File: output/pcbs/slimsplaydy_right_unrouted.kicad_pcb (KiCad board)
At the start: 2 copper layers, 117.1 x 87.4 mm, 24 parts

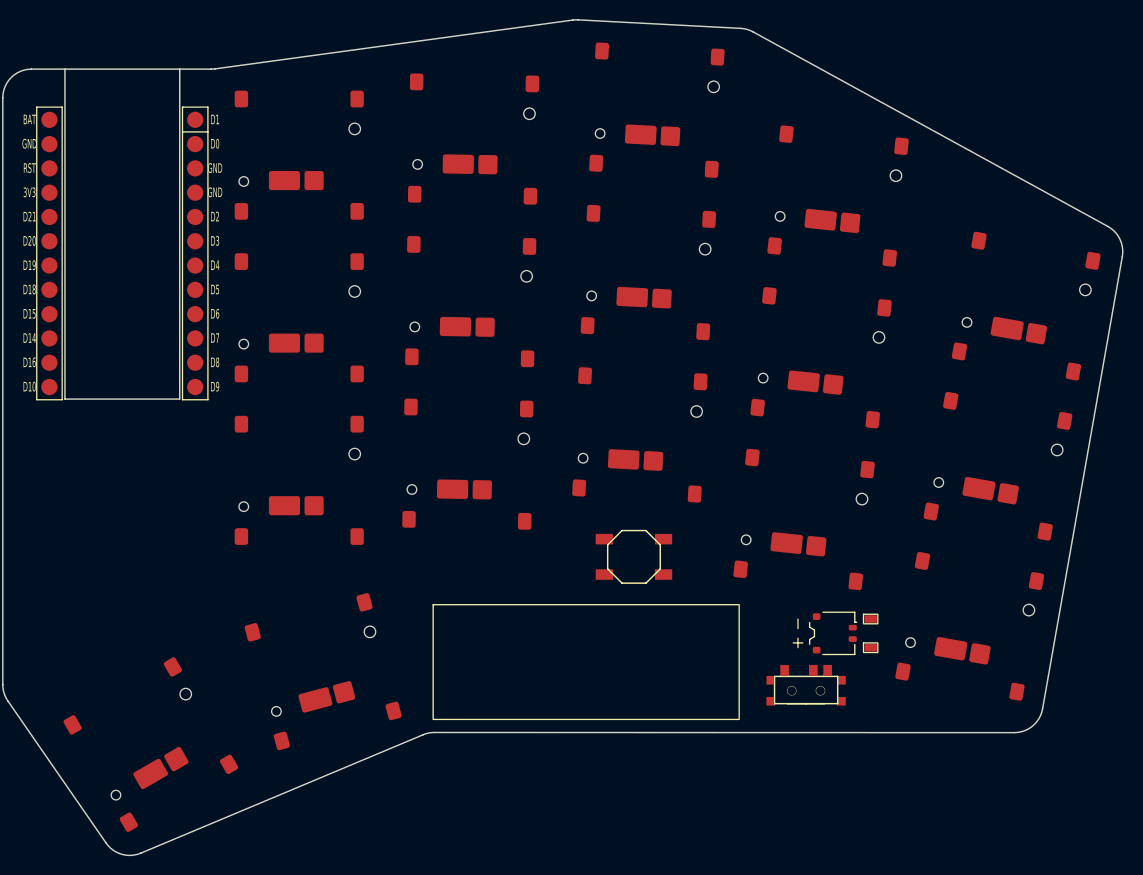
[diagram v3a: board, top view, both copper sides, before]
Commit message: Change weird 5/28 roundrect ratios to 1/8
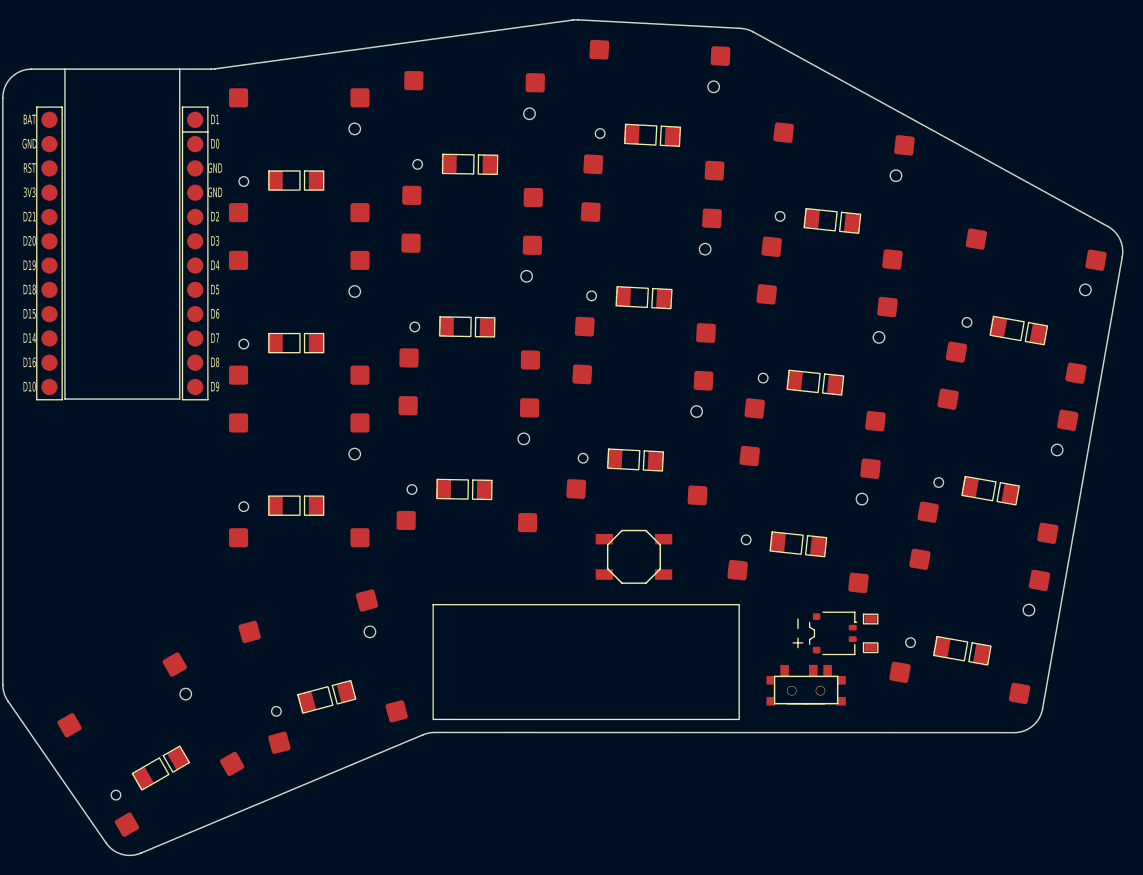
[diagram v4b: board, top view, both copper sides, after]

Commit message: Add logic to only place vias once when board is reversible; fix mispellings of reversible.
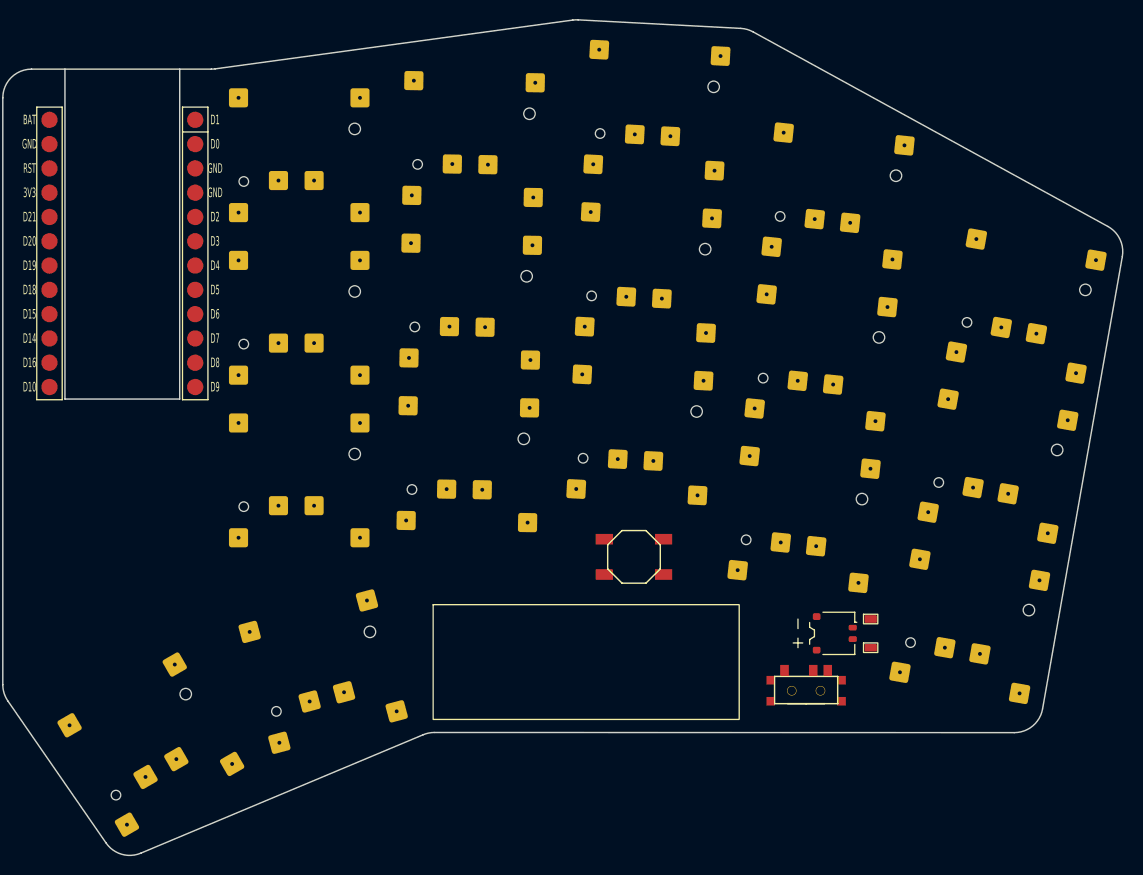
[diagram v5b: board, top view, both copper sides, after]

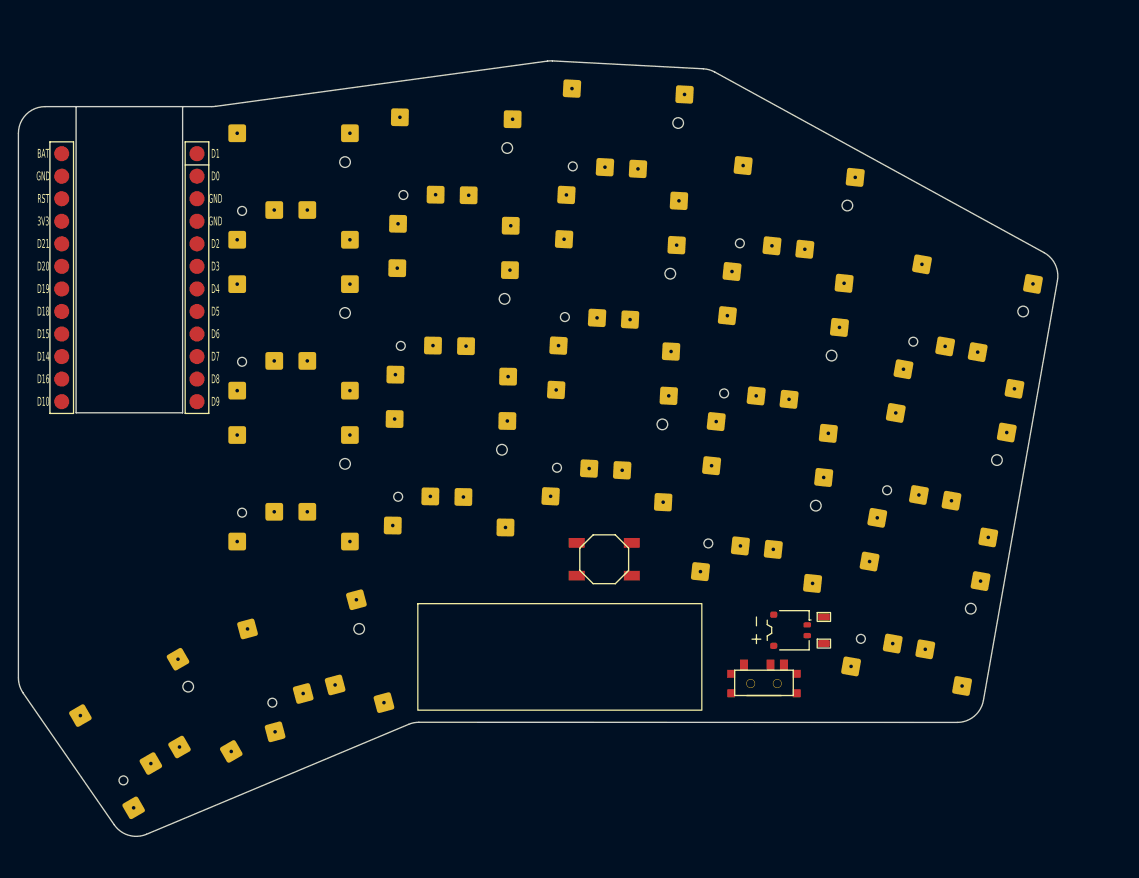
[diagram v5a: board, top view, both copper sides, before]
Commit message: Reposition battery/connector, work on mounting holes.
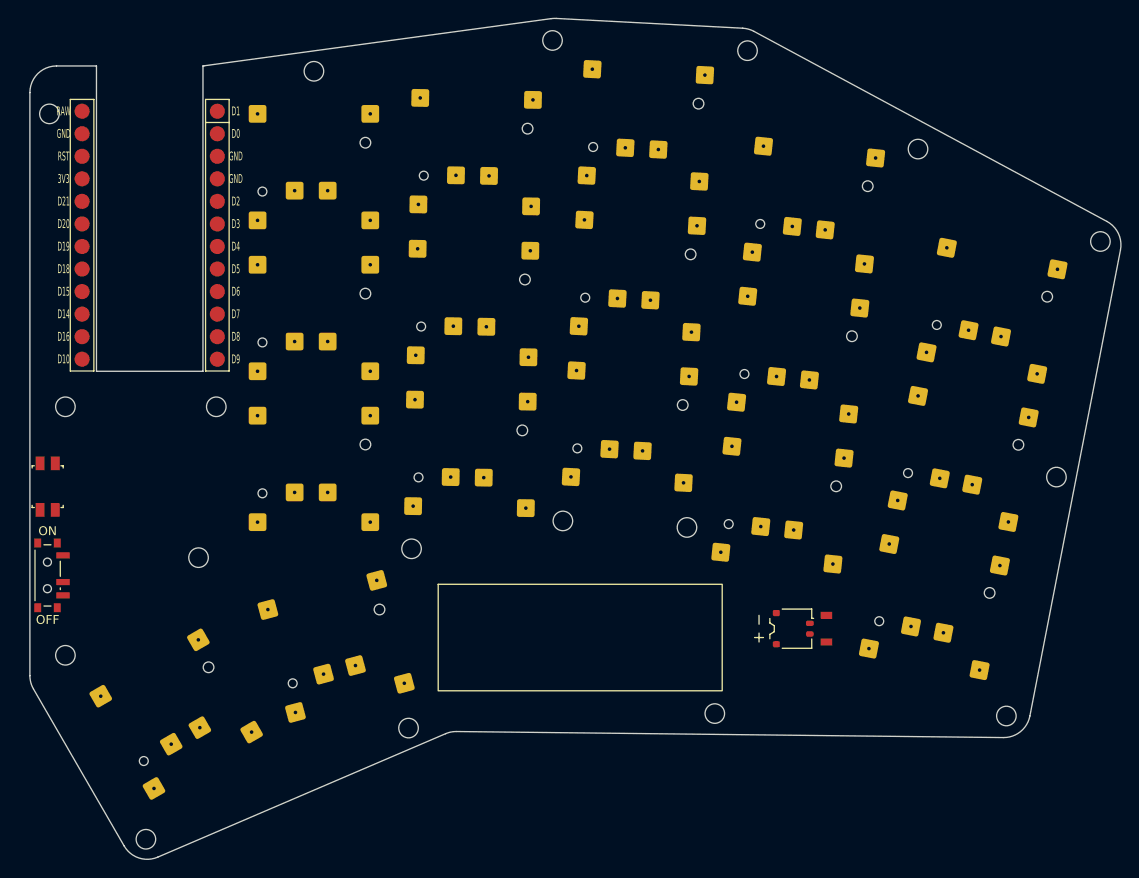
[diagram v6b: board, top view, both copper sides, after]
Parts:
- removed B1: , E73:SW_TACT_ALPS_SKQGABE010
- removed T1: , E73:SPDT_C128955
- removed XX2: , Pad_Single
- removed XX3: , Battery_301230
- added MH1: , ceoloide:mounting_hole_npth, F.Cu at (261.0, 81.4)
- added MH10: , ceoloide:mounting_hole_npth, F.Cu at (289.1, 132.1)
- added MH11: , ceoloide:mounting_hole_npth, F.Cu at (303.0, 132.8)
- added MH12: , ceoloide:mounting_hole_npth, F.Cu at (306.2, 153.8)
- added MH13: , ceoloide:mounting_hole_npth, F.Cu at (339.0, 154.1)
- added MH14: , ceoloide:mounting_hole_npth, F.Cu at (344.7, 127.1)
- added MH15: , ceoloide:mounting_hole_npth, F.Cu at (349.6, 100.6)
- added MH16: , ceoloide:mounting_hole_npth, F.Cu at (329.1, 90.2)
- added MH17: , ceoloide:mounting_hole_npth, F.Cu at (309.9, 79.1)
- added MH18: , ceoloide:mounting_hole_npth, F.Cu at (287.9, 78.0)
- added MH2: , ceoloide:mounting_hole_npth, F.Cu at (231.2, 86.2)
- added MH3: , ceoloide:mounting_hole_npth, F.Cu at (250.0, 119.2)
- added MH4: , ceoloide:mounting_hole_npth, F.Cu at (233.0, 119.2)
- added MH5: , ceoloide:mounting_hole_npth, F.Cu at (248.0, 136.2)
- added MH6: , ceoloide:mounting_hole_npth, F.Cu at (233.0, 147.2)
- added MH7: , ceoloide:mounting_hole_npth, F.Cu at (242.1, 168.0)
- added MH8: , ceoloide:mounting_hole_npth, F.Cu at (271.7, 155.4)
- added MH9: , ceoloide:mounting_hole_npth, F.Cu at (272.0, 135.2)
- added PAD1: , SMDPad, F.Cu at (318.8, 142.7)
- added PAD2: , SMDPad, F.Cu at (318.8, 145.7)
- added PWR1: , ceoloide:power_switch_smd_side, F.Cu at (231.0, 138.2)
- added RST1: , ceoloide:reset_switch_smd_side, F.Cu at (231.0, 128.2)
- XX1: footprint Pad_Single -> Battery_301230
- moved XX1 27.6 mm to (291.0, 145.2)
- moved MCU1 5.30 mm to (242.5, 98.6)
- moved S3 3.21 mm to (337.4, 108.4), turned to -11 degrees
- moved S6 3.17 mm to (317.3, 96.5)
- moved S15 3.17 mm to (261.0, 92.2)
- moved S4 3.17 mm to (313.8, 130.3)
- moved S13 3.17 mm to (261.0, 126.2)
- moved S14 3.17 mm to (261.0, 109.2)
- moved S16 3.17 mm to (263.5, 146.2)
- moved S5 3.17 mm to (315.6, 113.4)
- moved S7 3.17 mm to (296.6, 121.5)
- moved S9 3.17 mm to (298.4, 87.5)
- moved S8 3.17 mm to (297.5, 104.5)
- moved S17 3.17 mm to (245.5, 153.9)
- moved S12 3.17 mm to (279.2, 90.5)
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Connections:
- MCU1 pad 24: BAT -> RAW
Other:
- board size 117.1 x 87.4 mm -> 122.9 x 94.7 mm

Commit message: Finish up mounting, add case outlines, export step.
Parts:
- moved S12 178.9 mm to (170.2, -51.3)
- moved MH7 178.9 mm to (133.0, 26.2)
- moved S17 178.9 mm to (136.4, 12.1)
- moved MH15 178.9 mm to (240.6, -41.2)
- moved MH12 178.9 mm to (197.1, 12.0)
- moved MH14 178.9 mm to (235.6, -14.6)
- moved MH18 178.9 mm to (178.8, -63.8)
- moved S1 178.9 mm to (221.9, 0.00)
- moved S10 178.9 mm to (169.6, -17.3)
- moved S2 178.9 mm to (225.1, -16.7)
- moved S3 178.9 mm to (228.3, -33.4)
- moved S9 178.9 mm to (189.3, -54.3)
- moved CONN1 178.9 mm to (205.9, 2.43)
- moved MCU1 178.9 mm to (133.4, -43.2)
- moved MH1 178.9 mm to (151.9, -60.4)
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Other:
- net class Default removed

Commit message: Fix bug in PG1316S footprint causing vias in pads to not route correctly.
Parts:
- moved S12 178.9 mm to (279.2, 90.5)
- moved MH7 178.9 mm to (242.1, 168.0)
- moved S17 178.9 mm to (245.5, 153.9)
- moved MH15 178.9 mm to (349.6, 100.6)
- moved MH12 178.9 mm to (306.2, 153.8)
- moved MH14 178.9 mm to (344.7, 127.1)
- moved MH18 178.9 mm to (287.9, 78.0)
- moved S1 178.9 mm to (330.9, 141.8)
- moved S10 178.9 mm to (278.6, 124.5)
- moved S2 178.9 mm to (334.2, 125.1)
- moved S3 178.9 mm to (337.4, 108.4)
- moved S9 178.9 mm to (298.4, 87.5)
- moved CONN1 178.9 mm to (315.0, 144.2)
- moved MCU1 178.9 mm to (242.5, 98.6)
- moved MH1 178.9 mm to (261.0, 81.4)
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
